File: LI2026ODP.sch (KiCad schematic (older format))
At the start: 33 parts, among them J1 9-1437539-2, J2 Conn_01x05_Male, U1 LM2936MPX-3.0_NOPB, U2 STM32G0B1KET6, U3 max6921aui

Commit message: Change voltage regulator
from 3.0 to 3.3v
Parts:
- removed U1: LM2936MPX-3.0_NOPB, LM2936MXP:LM2936MPX-3.0&slash_NOPB, symbol LM2936:LM2936MPX-3.0_NOPB
- added U1: LM2936MM-3.3, LM2936MM:LM2936MM-3.3, symbol LM2936MM:LM2936MM-3.3
- C1: value C -> 4.7u
- C2, C3, C4: value C -> 0.1u
- R1, R2, R3, R4, R5, R6, R7, R8, R9: value R -> 15k
- R10, R12, R14: value R -> 27k
- R11, R13, R15: value R -> 3.3k
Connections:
- no-connect marks 29 -> 34
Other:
- moved on the sheet: C1

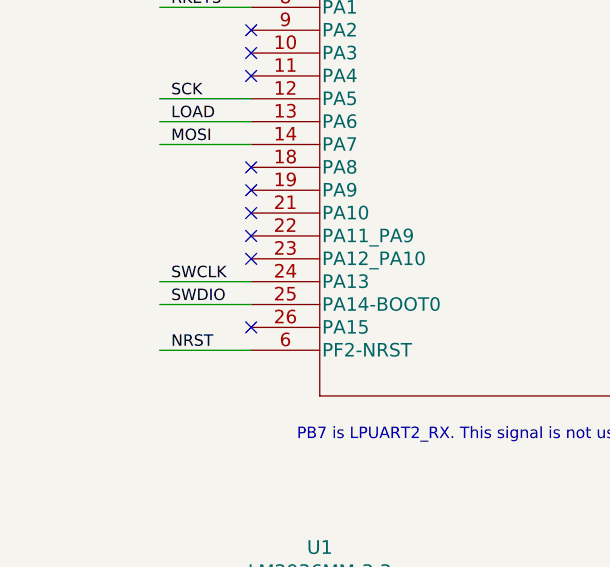
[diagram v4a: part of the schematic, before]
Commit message: Clean up the wire in the power layer.
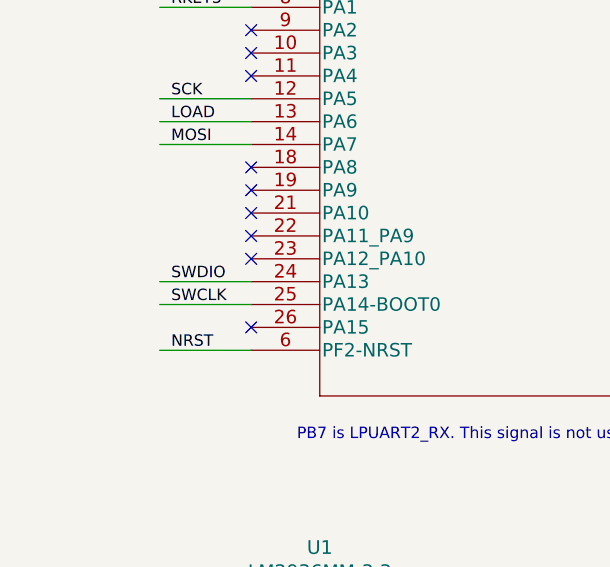
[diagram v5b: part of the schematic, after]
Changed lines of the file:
@@
 Wire Wire Line
 	1650 4000 1250 4000
-Text Label 1300 3900 0    50   ~ 0
-SWCLK
-Text Label 1300 4000 0    50   ~ 0
-SWDIO
 Wire Wire Line
 	5500 1850 5250 1850
@@
 NoConn ~ 1150 5950
 NoConn ~ 1150 6050
+Text Label 1300 3900 0    50   ~ 0
+SWDIO
+Text Label 1300 4000 0    50   ~ 0
+SWCLK
 $EndSCHEMATC
